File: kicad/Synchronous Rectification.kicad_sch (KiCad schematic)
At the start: 30 parts, among them Q8 BSC027N06LS5ATMA1, Q9 BSC027N06LS5ATMA1, U5 NCP4305DMTTWG, U8 NCP4305DMTTWG

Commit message: IMPORTANT NOTICE see #10 and fix in iBom
IMPORTANT NOTICE: There was a complaint about the converter not being rules conform. Due to other personal priorities it might take some weeks to solve the addressed points. There is also the chance of some points unable to be resolved. See #10 for further details.
iBom: There were some components missing in the iBom for PCBA.
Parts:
- C10, C25, C31, C6, C7, C9, NT1, NT2, Q8, Q9, R13, R14, R19, R20, R29, R30, R32, R33, R38, R40, R42, R43, TP1, TP2, TP3, TP4, TP5, TP6: ignore for iBOM (none) -> 1; ignore for iBom 1 -> (none)

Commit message: large DCDCv9-3r1.4 release update
- Removed some tables in csv and ods format (xlsx preferred)
- fixed issue #10 (waiting for approval)
- added video of adhesive testing for ESG10C-20G
- added video of primary and secondary winding
- updated all documentation files incl. Scrutineering Support Presentation
- updated transformer isolator part
- updated build notes
- updated README.md
- updated HV input connector
- added note about the discontinuation of the German versions
- added R75 onto the PCB (not required to solder on top of R31 anymore)
- updated iBoms and comments
- removed solder mask between TS an LV for better inspection
- replaced J1, unified crimps for all molex housings
- replaced U1
- fresh production files and gerber PDF plots
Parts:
- C10, C25, C31, C6, C7, C9, NT1, NT2, Q8, Q9, R13, R14, R19, R20, R29, R30, R32, R33, R38, R40, R42, R43, TP1, TP2, TP3, TP4, TP5, TP6: ignore for iBOM 1 -> (none); ignore for iBOM PCBA (none) -> 1
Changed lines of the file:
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@@
 			)
 		)
-		(property "ignore for iBOM" "1"
+		(property "ignore for iBOM PCBA" "1"
 			(at 40.64 111.125 0)
 			(effects
@@
 			)
 		)
-		(property "ignore for iBOM" "1"
+		(property "ignore for iBOM PCBA" "1"
 			(at 107.315 68.58 0)
 			(effects
@@
 			)
 		)
-		(property "ignore for iBOM" "1"
+		(property "ignore for iBOM PCBA" "1"
 			(at 90.805 129.54 0)
 			(effects
@@
 			)
 		)
-		(property "ignore for iBOM" "1"
+		(property "ignore for iBOM PCBA" "1"
 			(at 59.055 104.14 0)
 			(effects
@@
 			)
 		)
-		(property "ignore for iBOM" "1"
+		(property "ignore for iBOM PCBA" "1"
 			(at 40.64 61.595 0)
 			(effects
@@
 			)
 		)
-		(property "ignore for iBOM" "1"
+		(property "ignore for iBOM PCBA" "1"
 			(at 112.395 118.745 0)
 			(effects
@@
 			)
 		)
-		(property "ignore for iBOM" "1"
+		(property "ignore for iBOM PCBA" "1"
 			(at 97.79 53.975 0)
 			(effects
@@
 			)
 		)
-		(property "ignore for iBOM" "1"
+		(property "ignore for iBOM PCBA" "1"
 			(at 40.64 72.39 0)
 			(effects
@@
 			)
 		)
-		(property "ignore for iBOM" "1"
+		(property "ignore for iBOM PCBA" "1"
 			(at 40.64 122.555 0)
 			(effects
@@
 			)
 		)
-		(property "ignore for iBOM" "1"
+		(property "ignore for iBOM PCBA" "1"
 			(at 97.79 78.105 0)
 			(effects
@@
 			)
 		)
-		(property "ignore for iBOM" "1"
+		(property "ignore for iBOM PCBA" "1"
 			(at 59.055 53.975 0)
 			(effects
@@
 			)
 		)
-		(property "ignore for iBOM" "1"
+		(property "ignore for iBOM PCBA" "1"
 			(at 112.395 68.58 0)
 			(effects
@@
 			)
 		)
-		(property "ignore for iBOM" "1"
+		(property "ignore for iBOM PCBA" "1"
 			(at 118.745 135.255 0)
 			(effects
@@
 			)
 		)
-		(property "ignore for iBOM" "1"
+		(property "ignore for iBOM PCBA" "1"
 			(at 97.79 59.69 0)
 			(effects
@@
 			)
 		)
-		(property "ignore for iBOM" "1"
+		(property "ignore for iBOM PCBA" "1"
 			(at 107.315 118.745 0)
 			(effects
@@
 			)
 		)
-		(property "ignore for iBOM" "1"
+		(property "ignore for iBOM PCBA" "1"
 			(at 133.35 81.28 0)
 			(effects
@@
 			)
 		)
-		(property "ignore for iBOM" "1"
+		(property "ignore for iBOM PCBA" "1"
 			(at 110.49 135.255 0)
 			(effects
@@
 			)
 		)
-		(property "ignore for iBOM" "1"
+		(property "ignore for iBOM PCBA" "1"
 			(at 53.975 129.54 0)
 			(effects
@@
 			)
 		)
-		(property "ignore for iBOM" "1"
+		(property "ignore for iBOM PCBA" "1"
 			(at 110.49 85.725 0)
 			(effects
@@
 			)
 		)
-		(property "ignore for iBOM" "1"
+		(property "ignore for iBOM PCBA" "1"
 			(at 133.35 130.81 0)
 			(effects
@@
 			)
 		)
-		(property "ignore for iBOM" "1"
+		(property "ignore for iBOM PCBA" "1"
 			(at 59.055 79.375 0)
 			(effects
@@
 			)
 		)
-		(property "ignore for iBOM" "1"
+		(property "ignore for iBOM PCBA" "1"
 			(at 97.155 109.22 0)
 			(effects
@@
 			)
 		)
-		(property "ignore for iBOM" "1"
+		(property "ignore for iBOM PCBA" "1"
 			(at 118.745 85.725 0)
 			(effects
@@
 			)
 		)
-		(property "ignore for iBOM" "1"
+		(property "ignore for iBOM PCBA" "1"
 			(at 97.155 128.27 0)
 			(effects
@@
 			)
 		)
-		(property "ignore for iBOM" "1"
+		(property "ignore for iBOM PCBA" "1"
 			(at 97.155 103.505 0)
 			(effects
@@
 			)
 		)
-		(property "ignore for iBOM" "1"
+		(property "ignore for iBOM PCBA" "1"
 			(at 53.975 79.375 0)
 			(effects
@@
 			)
 		)
-		(property "ignore for iBOM" "1"
+		(property "ignore for iBOM PCBA" "1"
 			(at 59.055 129.54 0)
 			(effects
@@
 			)
 		)
-		(property "ignore for iBOM" "1"
+		(property "ignore for iBOM PCBA" "1"
 			(at 90.805 81.915 0)
 			(effects

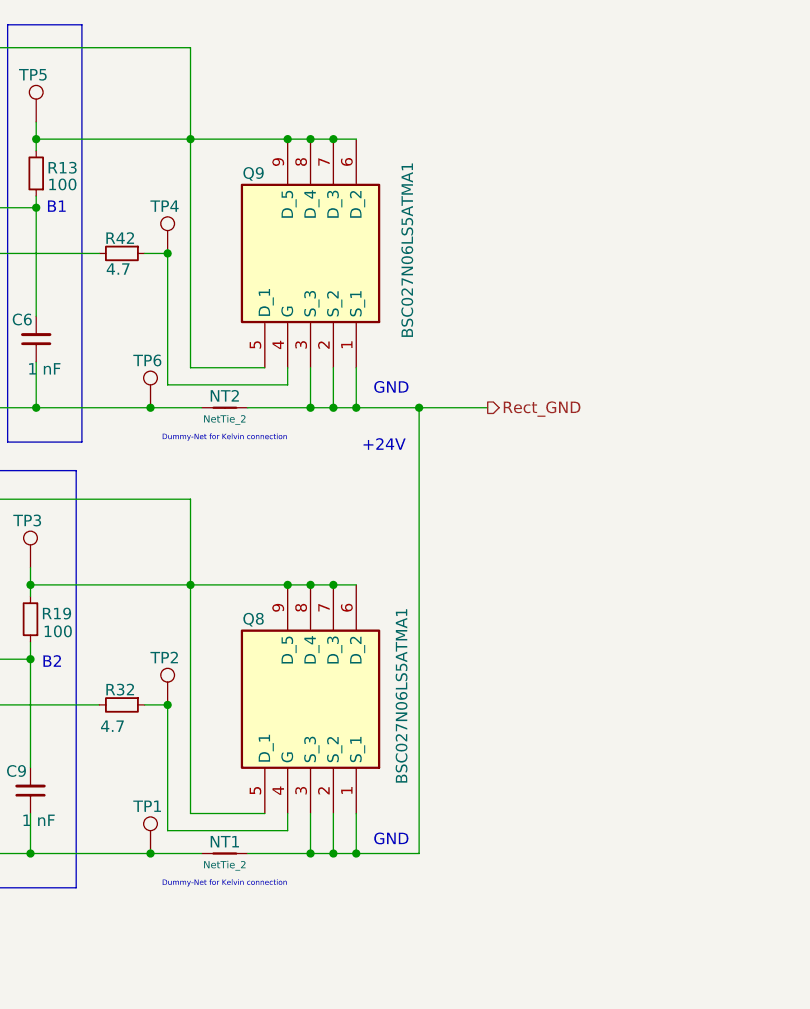
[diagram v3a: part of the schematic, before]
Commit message: testing new components for a v9-4. Not recommended for manufacturing!
Replaced: D14, U1, U11, Q8, Q9, Q10, Q11
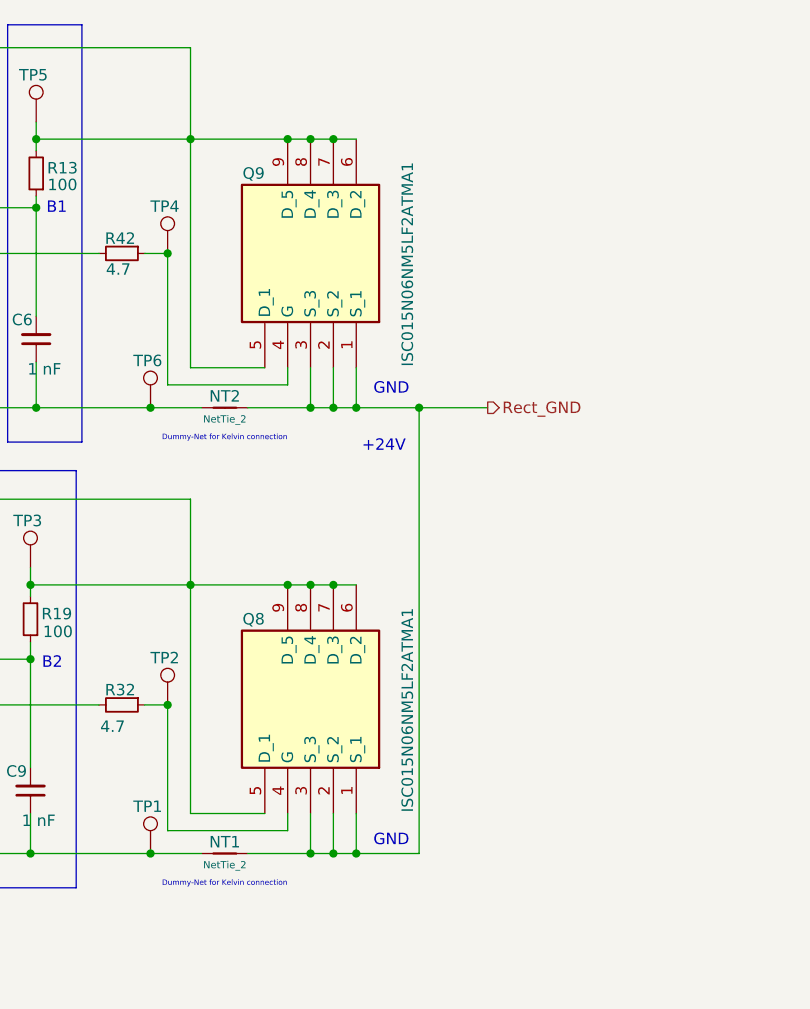
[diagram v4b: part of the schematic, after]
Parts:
- Q8, Q9: value BSC027N06LS5ATMA1 -> ISC015N06NM5LF2ATMA1; Manufacturer_Part_Number BSC027N06LS5ATMA1 -> ISC015N06NM5LF2ATMA1; Mouser Part Number 726-BSC027N06LS5ATMA -> 726-ISC015N06NM5LF2A

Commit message: added PCBA BOM, added lots of JLC part numbers
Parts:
- C10, C7: JLCPCB Part # (none) -> C22440592; Manufacturer_Part_Number 885342208005 -> VJ1206A471JXGTW1HV
- C25, C31: JLCPCB Part # (none) -> C15849
- C6, C9: JLCPCB Part # (none) -> C342954; Manufacturer_Part_Number SH31B102K631CT -> VJ1206A102KXGTW1HV
- Q8, Q9: JLCPCB Part # (none) -> C24491072
- R32, R42: JLCPCB Part # (none) -> C313986
